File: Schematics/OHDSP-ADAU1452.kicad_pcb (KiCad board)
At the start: 4 copper layers, 100 x 100 mm, 294 parts, among them CN201 COAX, CN401 COAX, CN402 COAX, CN405 COAX, CN406 COAX, P201 CONN_2x1, P203 CONN_6X2, P204 CONN_6x1, P301 CONN_2x1, P302 CONN_2x1, P303 PIN, P304 PIN, P305 PIN, P306 PIN, P601 CONN_02X05, P602 CONN_02X05, P603 CONN_02X05, P604 CONN_02X05, P605 CONN_3x1, P606 CONN_6X2, P607 CONN_02X05, P608 CONN_02X05, P609 CONN_02X20, P610 CONN_02X05, P611 CONN_5x1, P613 CONN_02X05, P614 CONN_02X05, P615 CONN_02X05, P616 CONN_02X05, SW202 SWITCH, U201 ADAU1452WBCPZ, U202 ADM13307-5ARZ, U203 25AA1024, U301 IC-REG-XRP7659ISTR-F, U302 IC-REG-XRP7659ISTR-F, U304 IC-REG-XC6210B332MR, U305 IC-REG-XC6210B332MR, U401 NB3L553, U501 IC-SPDIF-RX-OPTO, U502 IC-SPDIF-TX-OPTO, X201 24M576

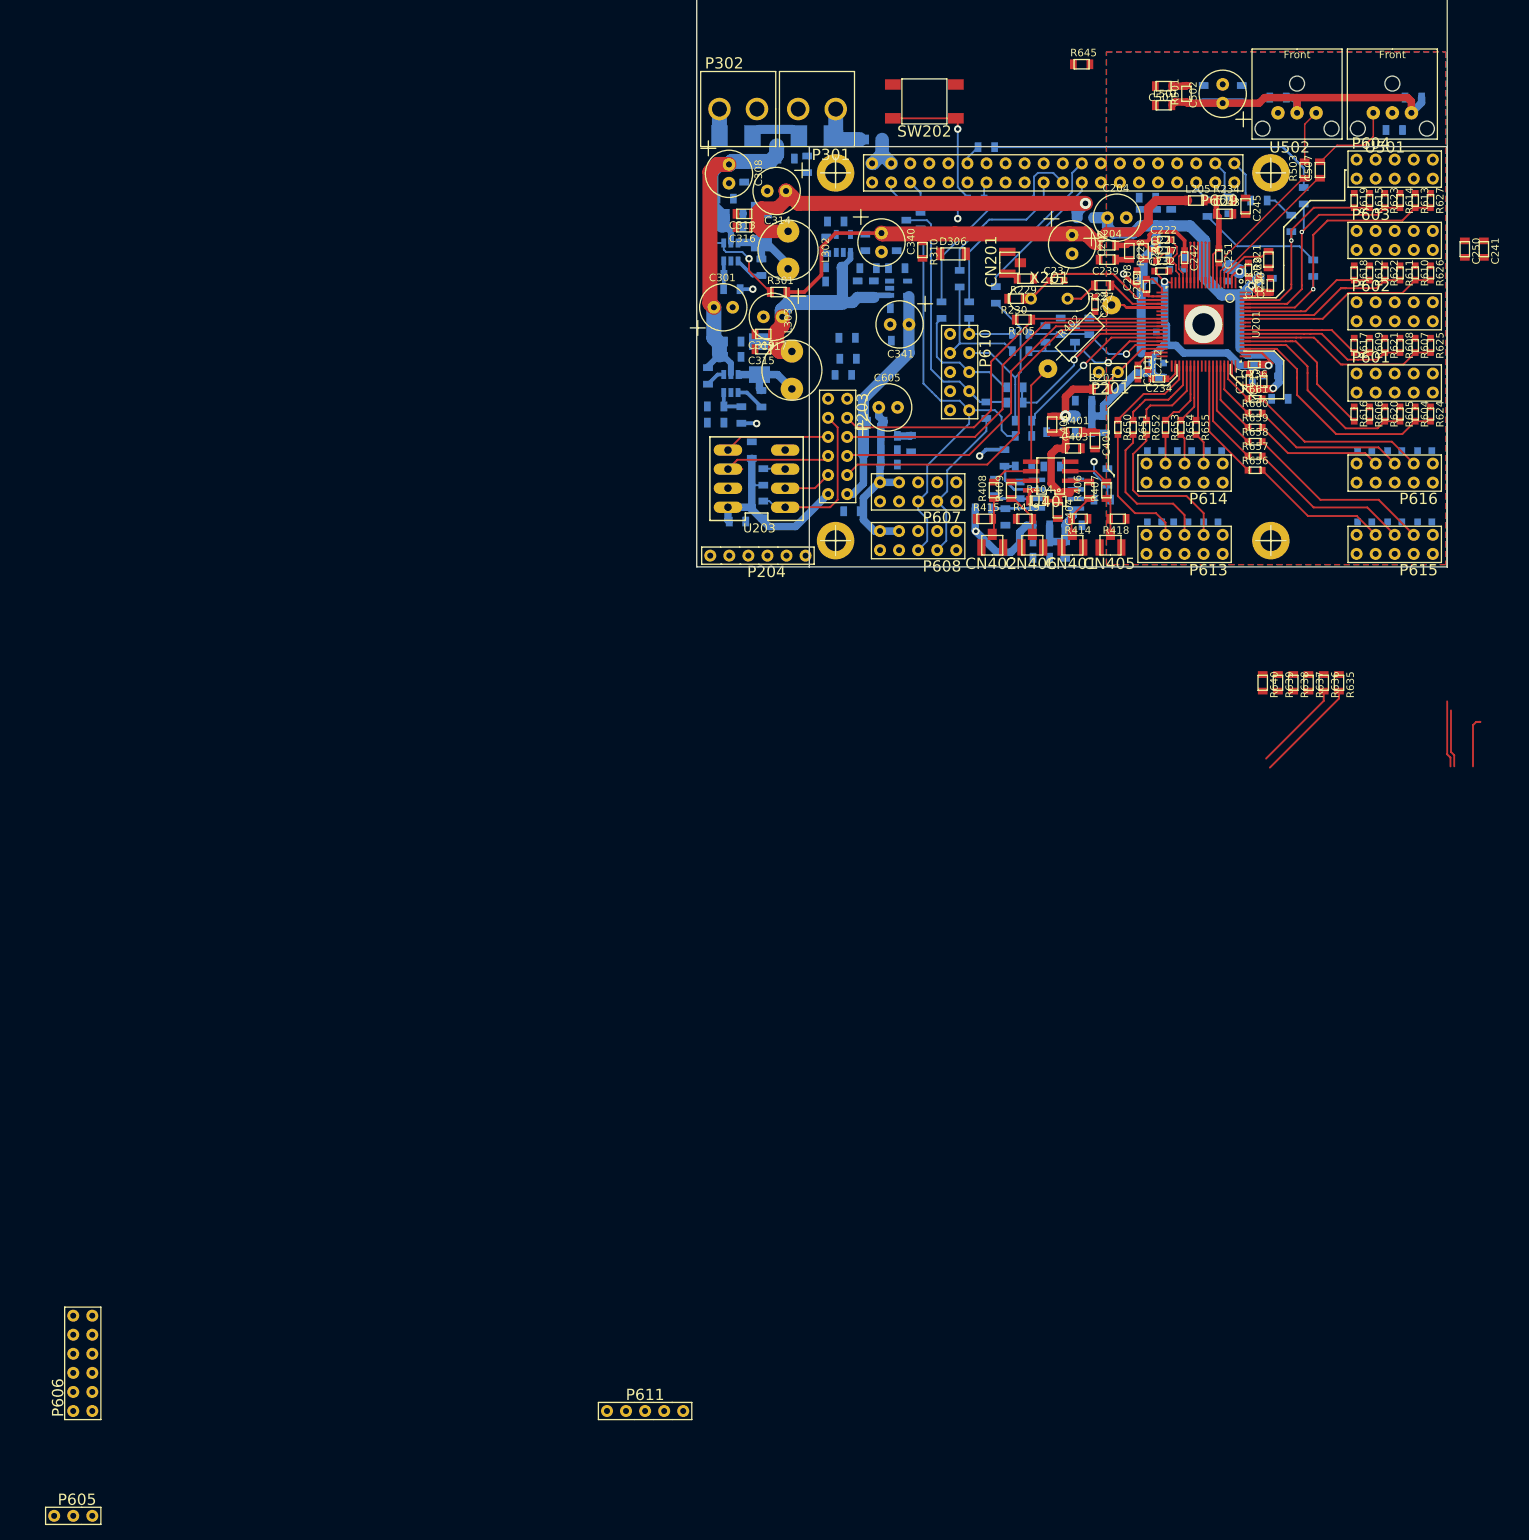
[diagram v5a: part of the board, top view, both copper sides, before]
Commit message: PCB work, removed pointless connector
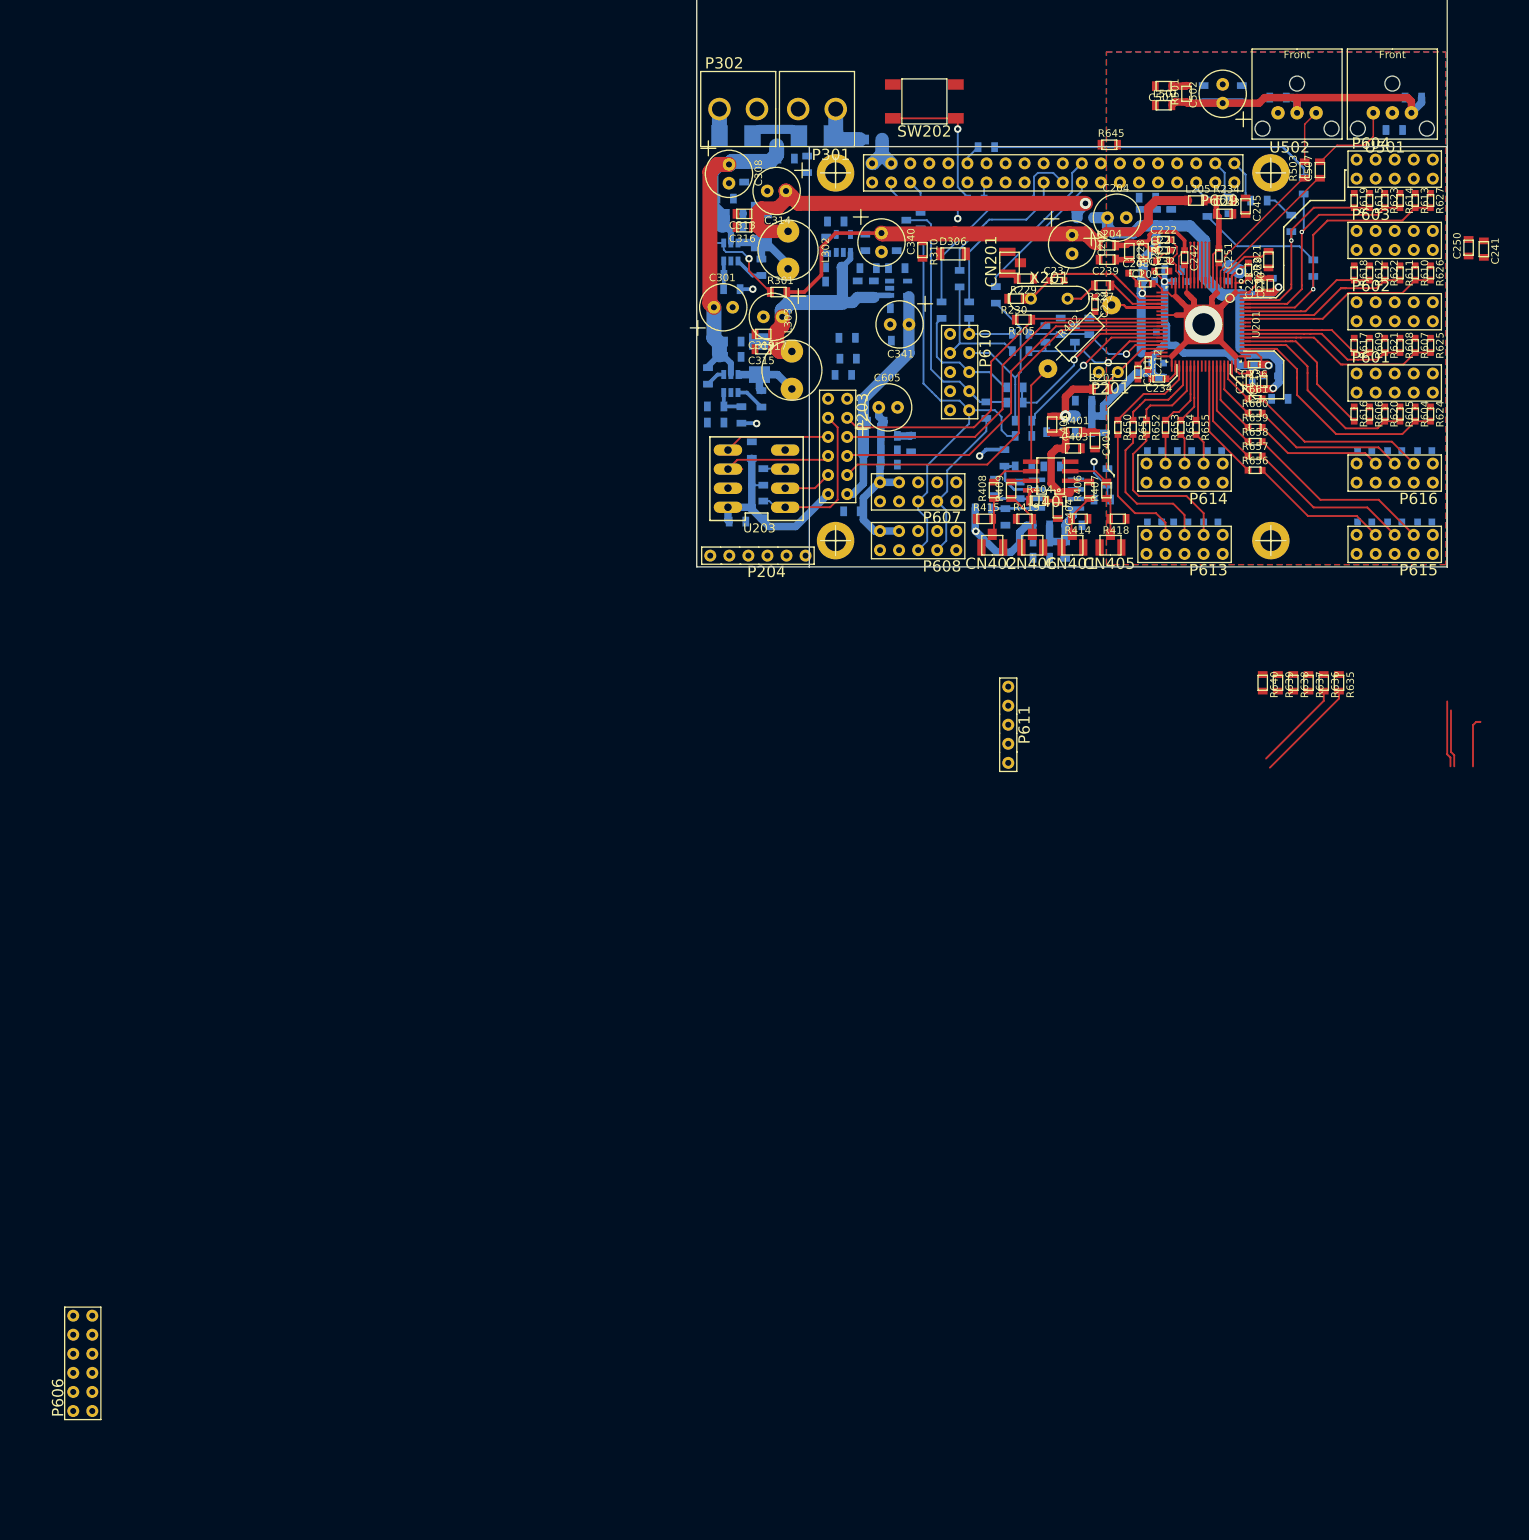
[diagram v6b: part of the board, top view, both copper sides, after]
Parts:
- removed P605: CONN_3x1, OHDSP-Footprints-Pretty:CONN_SIL_3
- moved P611 110.3 mm to (246.5, 140.0), turned to 270 degrees
- moved R645 11.3 mm to (260.0, 67.8)
- moved C225 1.85 mm to (268.5, 84.5)
- moved C230 1.73 mm to (269.5, 86.0)
- moved R602 1.33 mm to (285.9, 73.2)
- moved C208 0.63 mm to (263.5, 84.9), turned to 0 degrees
- moved C250 0.54 mm to (307.8, 81.5), turned to 90 degrees
- moved C209 0.38 mm to (264.7, 86.3), turned to 0 degrees
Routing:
- net GNDD: track 8.45 -> 108.0 mm
- net /ADAU1452/ADCIN_BCLK3: track 34.2 -> 35.5 mm
- net /Connectors/RPI_BCLK: track 48.9 -> 47.5 mm
- net /ADAU1452/DVDD: track 90.7 -> 91.4 mm
- net /ADAU1452/IOVDD: track 74.7 -> 75.3 mm

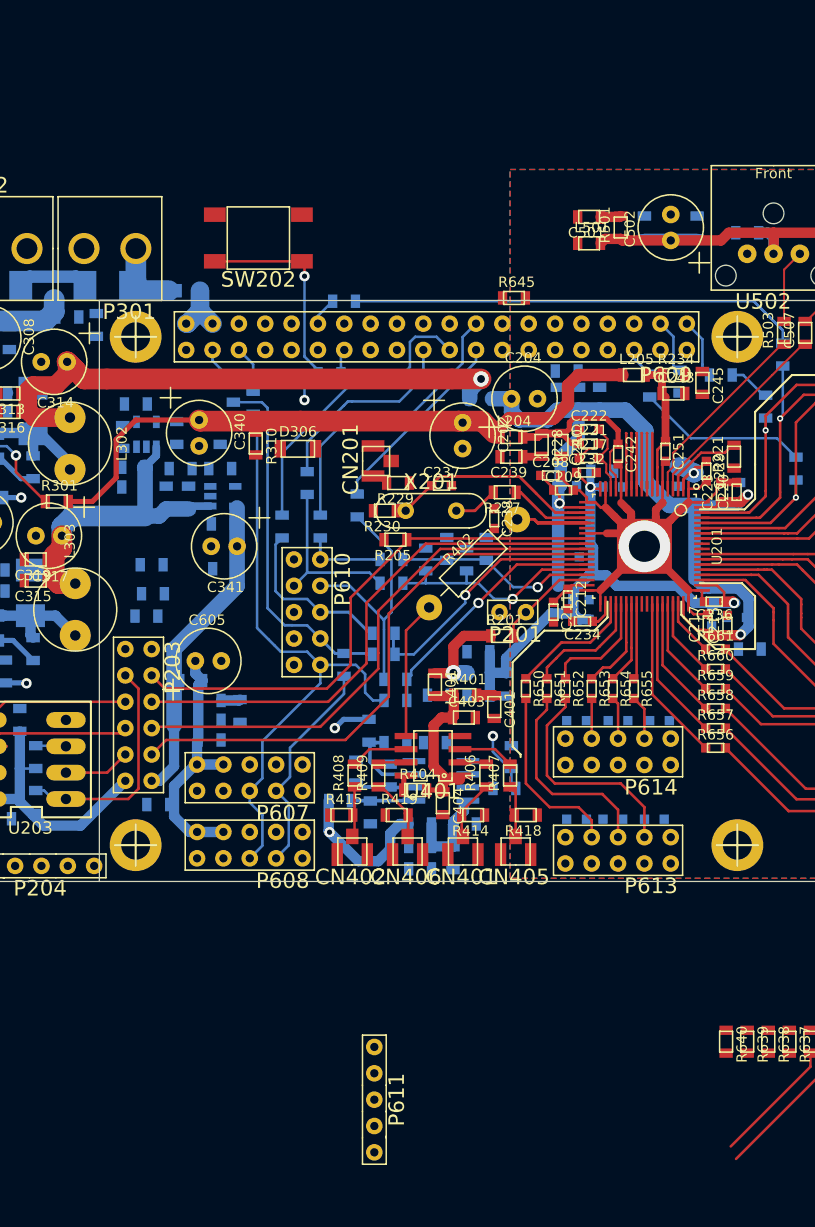
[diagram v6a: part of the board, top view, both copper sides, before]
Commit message: PCB work, extra Pi GPIO to external connectors
PCB work, extra Pi GPIO to external connectors
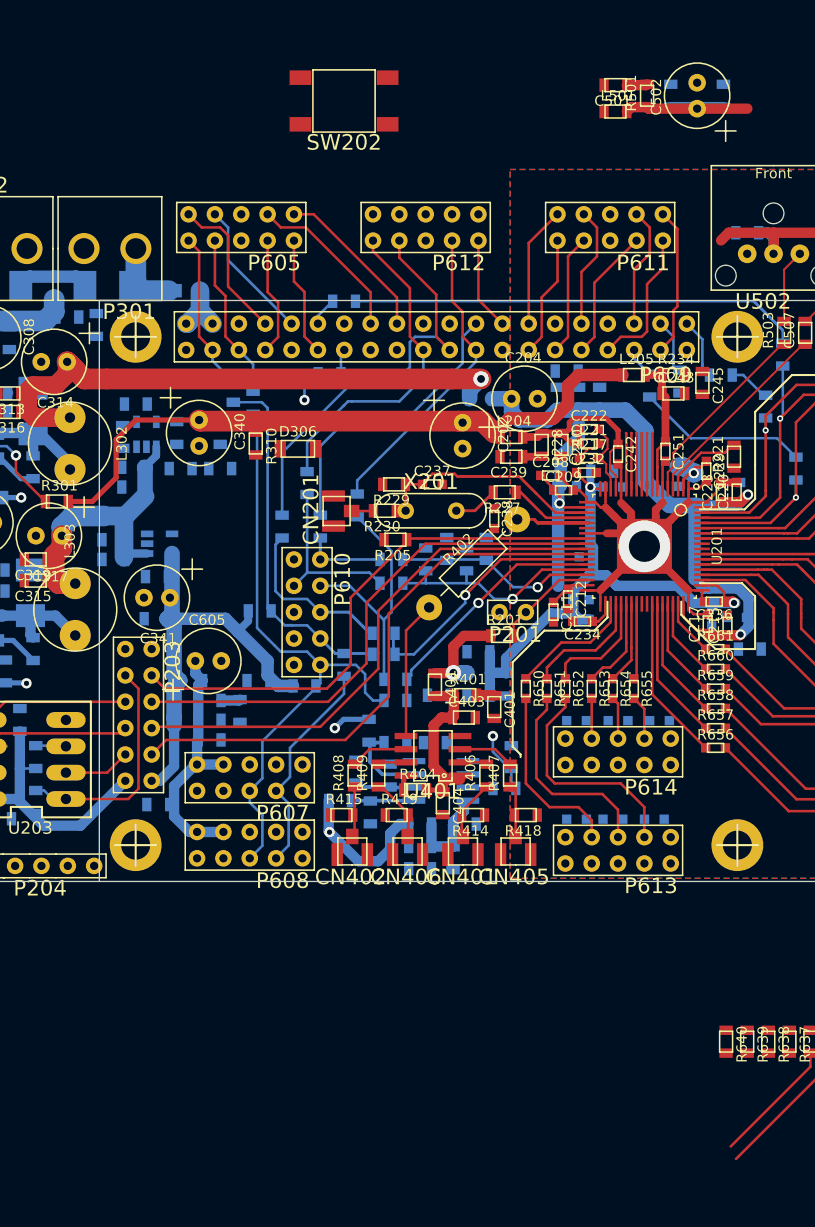
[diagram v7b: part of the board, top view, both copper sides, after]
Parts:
- removed R645: 0R, OHDSP-Footprints-Pretty:SMD-0805
- added P605: CONN_02X05, OHDSP-Footprints-Pretty:CONN_DIL_2X5, F.Cu at (233.7, 61.0)
- added P612: CONN_02X05, OHDSP-Footprints-Pretty:CONN_DIL_2X5, F.Cu at (251.5, 61.0)
- P611: value CONN_5x1 -> CONN_02X05; footprint OHDSP-Footprints-Pretty:CONN_SIL_5 -> OHDSP-Footprints-Pretty:CONN_DIL_2X5
- moved P611 82.2 mm to (269.2, 61.0), turned to 90 degrees
- moved R202 18.8 mm to (239.8, 105.2)
- moved SW202 15.6 mm to (243.6, 48.8)
- moved C201 13.2 mm to (235.3, 104.6)
- moved C502 13.0 mm to (277.6, 48.3)
- moved C504 13.0 mm to (275.1, 48.3)
- moved R501 13.0 mm to (272.8, 48.3)
- moved C501 13.0 mm to (269.7, 47.2)
- moved C503 13.0 mm to (280.2, 48.3)
- moved L501 13.0 mm to (269.7, 49.8)
- moved R203 10.9 mm to (235.5, 97.9)
- moved C326 9.38 mm to (221.4, 93.0), turned to 180 degrees
- moved C338 8.18 mm to (225.4, 98.7)
- moved C341 8.15 mm to (225.6, 96.6)
- moved C335 8.13 mm to (225.6, 94.6)
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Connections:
- net Net-(P609-Pad15) renamed /Connectors/PI_GP22
- net Net-(P609-Pad19) renamed /Connectors/PI_MOSI
- net Net-(P609-Pad21) renamed /Connectors/PI_MISO
- net Net-(P609-Pad23) renamed /Connectors/PI_SCLK
- net Net-(P609-Pad3) renamed /Connectors/PI_SDA
- net Net-(P609-Pad5) renamed /Connectors/PI_SCL
- P609 pad 10: Net-(P609-Pad10) -> /Connectors/PI_GP15
- P609 pad 11: Net-(P609-Pad11) -> /Connectors/PI_GP17
- P609 pad 16: Net-(P609-Pad16) -> /Connectors/PI_GP23
- P609 pad 18: Net-(P609-Pad18) -> /Connectors/PI_GP24
- P609 pad 26: Net-(P609-Pad26) -> /Connectors/RPI_CS2
- P609 pad 27: Net-(P609-Pad27) -> /Connectors/PI_IDSD
- P609 pad 28: Net-(P609-Pad28) -> /Connectors/PI_IDSC
- P609 pad 29: Net-(P609-Pad29) -> /Connectors/PI_GP5
- P609 pad 31: Net-(P609-Pad31) -> /Connectors/PI_GP6
- P609 pad 32: Net-(P609-Pad32) -> /Connectors/PI_GP12
- P609 pad 33: Net-(P609-Pad33) -> /Connectors/PI_GP13
- P609 pad 36: Net-(P609-Pad36) -> /Connectors/PI_GP16
- P609 pad 37: Net-(P609-Pad37) -> /Connectors/PI_GP26
- P609 pad 7: Net-(P609-Pad7) -> /Connectors/PI_GP4
- P609 pad 8: Net-(P609-Pad8) -> /Connectors/PI_GP14
- P611 pad 1: /ADAU1452/SPI_MOSI -> /Connectors/PI_IDSD
- P611 pad 2: /ADAU1452/SPI_SCLK -> /Connectors/PI_IDSC
- P611 pad 3: /ADAU1452/SPI_MISO -> /Connectors/PI_GP5
- P611 pad 4: /ADAU1452/SPI_~CS -> /Connectors/PI_GP12
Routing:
- net /ADAU1452/MRST: track 72.1 -> 52.6 mm, vias 3 -> 2
- net /Connectors/PI_GP23: track 0.00 -> 16.1 mm
- net /Connectors/PI_GP24: track 0.00 -> 15.8 mm
- net /Connectors/PI_GP14: track 0.00 -> 14.6 mm
- net /Connectors/PI_GP26: track 0.00 -> 14.3 mm
- net /Connectors/PI_GP13: track 0.00 -> 13.9 mm
- net /Connectors/PI_GP15: track 0.00 -> 13.6 mm
- net /Connectors/PI_GP6: track 0.00 -> 12.7 mm
- net /Connectors/PI_MISO: track 28.7 -> 41.3 mm
- net /Connectors/PI_MOSI: track 19.3 -> 31.8 mm
- net /Connectors/PI_IDSC: track 0.00 -> 11.7 mm
- net /Connectors/PI_GP16: track 0.00 -> 11.7 mm
- net /Connectors/PI_GP12: track 0.00 -> 11.7 mm
- net /Connectors/PI_IDSD: track 0.00 -> 11.7 mm
- net /Connectors/PI_GP5: track 0.00 -> 11.7 mm
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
